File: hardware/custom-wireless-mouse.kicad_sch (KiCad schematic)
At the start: 34 parts, among them J1 SWD_HEADER, J2 B2B-XH-A, Q1 DMG2305UXQ, SW1 JS202011SCQN, SW2 D2FC-F-7N(20M), SW3 D2FC-F-7N(20M), SW4 D2FC-F-7N(20M), SW5 D2FC-F-7N(20M), U1 nRF52810-QCAA-T, U2 PMW3610DM-SUDU, U3 TLV61220DBVT, Y1 NX2016SA-32MHZ

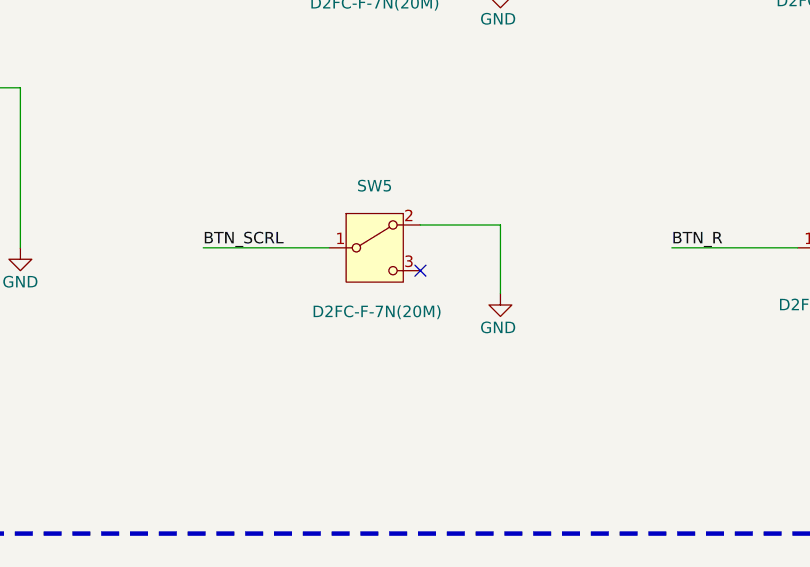
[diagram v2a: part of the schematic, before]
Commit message: Swap SW5 to a low-profile switch that clears the scroll wheel
SW5 (wheel middle-click) previously reused the same Omron D2FC-F-7N(20M)
as SW2-4, but that part's 6.5mm THT body doesn't fit underneath the
scroll wheel, which mounts on ENC1's shaft directly above it.

Deep-audited real, in-stock DigiKey.ca alternatives against the height
constraint and selected Omron B3U-1000P: 1.6mm actuator height, 2-pin
SPST-NO, exact-match footprint and 3D model already in KiCad's own
official library. Vendored the real datasheet, symbol, footprint, and
3D model; registered the new library; swapped SW5's schematic symbol,
footprint, and sourcing fields.

The old part's 3-pin COM/NO/NC wiring doesn't map onto the new part's
plain 2-pin SPST, so SW5's prior connections (to BTN_SCRL and GND) were
removed along with the old symbol rather than carried over incorrectly.
SW5 is intentionally left unwired pending manual rewiring and PCB
re-placement - documented in pinout.md and open-items.md. ERC confirms
the only fallout is the two now-expected unconnected pins on SW5.
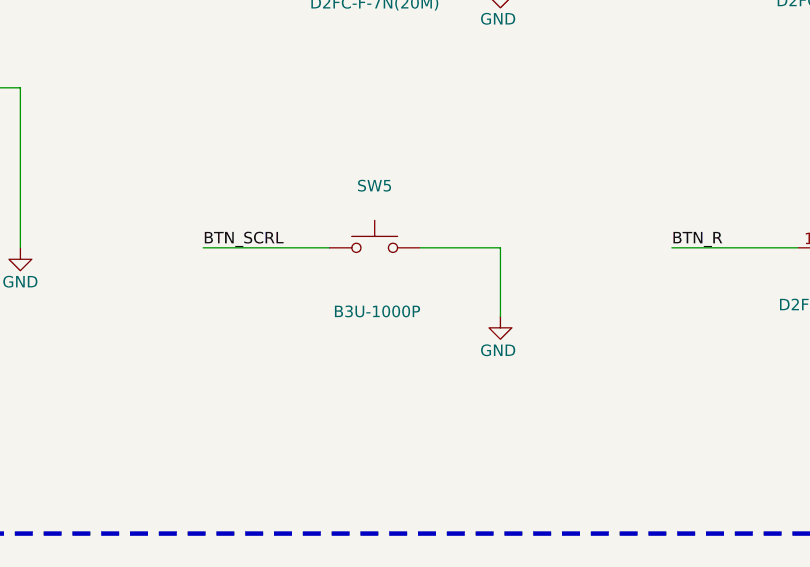
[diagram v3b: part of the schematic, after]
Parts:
- SW5: value D2FC-F-7N(20M) -> B3U-1000P; footprint omron-d2fc-f-7n:switch-tht-omron-d2fc-f-7n -> omron-b3u-1000p:switch-smd-omron-b3u-1000p; symbol omron-d2fc-f-7n:D2FC-F-7N-20M -> omron-b3u-1000p:B3U-1000P; DPN 39-D2FC-F-7N(20M)-ND -> SW1020CT-ND; MPN D2FC-F-7N(20M) -> B3U-1000P
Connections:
- no-connect marks 14 -> 13
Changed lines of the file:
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@@
 	)
 	(no_connect
-		(at 325.12 218.44)
-	)
-	(no_connect
 		(at 78.74 59.69)
 	)
@@
 	(wire
 		(pts
+			(xy 334.01 215.9) (xy 325.12 215.9)
+		)
+		(stroke
+			(width 0)
+			(type default)
+		)
+	)
+	(wire
+		(pts
 			(xy 113.03 213.36) (xy 139.7 213.36)
 		)
@@
 	(wire
 		(pts
-			(xy 314.96 215.9) (xy 300.99 215.9)
-		)
-		(stroke
-			(width 0)
-			(type default)
-		)
-	)
-	(wire
-		(pts
 			(xy 307.34 81.28) (xy 323.85 81.28)
 		)
@@
 	(wire
 		(pts
+			(xy 314.96 215.9) (xy 300.99 215.9)
+		)
+		(stroke
+			(width 0)
+			(type default)
+		)
+	)
+	(wire
+		(pts
 			(xy 346.71 35.56) (xy 346.71 38.1)
 		)
@@
 	(wire
 		(pts
+			(xy 334.01 215.9) (xy 334.01 223.52)
+		)
+		(stroke
+			(width 0)
+			(type default)
+		)
+	)
+	(wire
+		(pts
 			(xy 102.87 152.4) (xy 102.87 156.21)
 		)
@@
 	(wire
 		(pts
-			(xy 334.01 213.36) (xy 334.01 220.98)
-		)
-		(stroke
-			(width 0)
-			(type default)
-		)
-	)
-	(wire
-		(pts
 			(xy 246.38 100.33) (xy 229.87 100.33)
 		)
@@
 	(wire
 		(pts
-			(xy 334.01 213.36) (xy 325.12 213.36)
-		)
-		(stroke
-			(width 0)
-			(type default)
-		)
-	)
-	(wire
-		(pts
 			(xy 104.14 66.04) (xy 104.14 55.88)
 		)
@@
 		)
 	)
+	(label "BTN_SCRL"
+		(at 300.99 215.9 0)
+		(effects
+			(font
+				(size 1.27 1.27)
+			)
+			(justify left bottom)
+		)
+	)
 	(label "VBAT_SW"
 		(at 104.14 55.88 180)
@@
 		)
 	)
-	(label "BTN_SCRL"
-		(at 300.99 215.9 0)
-		(effects
-			(font
-				(size 1.27 1.27)
-			)
-			(justify left bottom)
-		)
-	)
 	(label "WHEEL_B"
 		(at 392.43 66.04 180)
@@
 	)
 	(symbol
-		(lib_id "omron-d2fc-f-7n:D2FC-F-7N-20M")
+		(lib_id "omron-b3u-1000p:B3U-1000P")
 		(at 320.04 215.9 0)
 		(unit 1)
@@
 			)
 		)
-		(property "Value" "D2FC-F-7N(20M)"
+		(property "Value" "B3U-1000P"
 			(at 320.294 223.012 0)
 			(show_name no)
@@
 			)
 		)
-		(property "Footprint" "omron-d2fc-f-7n:switch-tht-omron-d2fc-f-7n"
+		(property "Footprint" "omron-b3u-1000p:switch-smd-omron-b3u-1000p"
 			(at 320.04 215.9 0)
 			(hide yes)
@@
 			)
 		)
-		(property "Datasheet" "${KIPRJMOD}/datasheets/omron-d2f-family-datasheet.pdf"
+		(property "Datasheet" "${KIPRJMOD}/datasheets/omron-b3u-1000p-datasheet.pdf"
 			(at 320.04 215.9 0)
 			(hide yes)
@@
 			)
 		)
-		(property "Description" ""
+		(property "Description" "Ultra-small SMD tactile switch, SPST-NO, 1.6mm actuator height - low-profile wheel middle-click switch (swapped from D2FC-F-7N to clear the scroll wheel above it; UNWIRED, needs pin1/pin2 connected)"
 			(at 320.04 215.9 0)
+			(hide yes)
 			(show_name no)
 			(do_not_autoplace no)
@@
 			)
 		)
-		(property "MPN" "D2FC-F-7N(20M)"
+		(property "MPN" "B3U-1000P"
 			(at 0 0 0)
 			(hide yes)
@@
 			)
 		)
-		(property "DPN" "39-D2FC-F-7N(20M)-ND"
+		(property "DPN" "SW1020CT-ND"
 			(at 0 0 0)
 			(hide yes)
@@
 		(pin "2"
 		)
-		(pin "3"
-		)
 		(instances
 			(project "custom-wireless-mouse"
@@
 	(symbol
 		(lib_id "local:GND")
-		(at 334.01 220.98 0)
-		(unit 1)
-		(body_style 1)
-		(exclude_from_sim no)
-		(in_bom yes)
-		(on_board yes)
-		(in_pos_files yes)
-		(dnp no)
-		(property "Reference" "#PWR049"
-			(at 334.01 218.44 0)
-			(hide yes)
-			(show_name no)
-			(do_not_autoplace no)
-			(effects
-				(font
-					(size 1.27 1.27)
-				)
-			)
-		)
-		(property "Value" "GND"
-			(at 333.756 224.79 0)
-			(show_name no)
-			(do_not_autoplace no)
-			(effects
-				(font
-					(size 1.27 1.27)
-				)
-			)
-		)
-		(property "Footprint" ""
-			(at 334.01 220.98 0)
-			(hide yes)
-			(show_name no)
-			(do_not_autoplace no)
-			(effects
-				(font
-					(size 1.27 1.27)
-				)
-			)
-		)
-		(property "Datasheet" ""
-			(at 334.01 220.98 0)
-			(hide yes)
-			(show_name no)
-			(do_not_autoplace no)
-			(effects
-				(font
-					(size 1.27 1.27)
-				)
-			)
-		)
-		(property "Description" ""
-			(at 334.01 220.98 0)
-			(show_name no)
-			(do_not_autoplace no)
-			(effects
-				(font
-					(size 1.27 1.27)
-				)
-			)
-		)
-		(pin "1"
-		)
-		(instances
-			(project "custom-wireless-mouse"
-				(path "/d776ca83-3842-4947-ae63-5f40f232181f"
-					(reference "#PWR049")
-					(unit 1)
-				)
-			)
-		)
-	)
-	(symbol
-		(lib_id "local:GND")
 		(at 246.38 115.57 0)
 		(unit 1)
@@
 					(unit 1)
 				)
+			)
+		)
+	)
+	(symbol
+		(lib_id "local:GND")
+		(at 334.01 223.52 0)
+		(unit 1)
+		(body_style 1)
+		(exclude_from_sim no)
+		(in_bom yes)
+		(on_board yes)
+		(in_pos_files yes)
+		(dnp no)
+		(property "Reference" "#PWR041"
+			(at 334.01 220.98 0)
+			(hide yes)
+			(show_name no)
+			(do_not_autoplace no)
+			(effects
+				(font
+					(size 1.27 1.27)
+				)
+			)
+		)
+		(property "Value" "GND"
+			(at 333.756 227.33 0)
+			(show_name no)
+			(do_not_autoplace no)
+			(effects
+				(font
+					(size 1.27 1.27)
+				)
+			)
+		)
+		(property "Footprint" ""
+			(at 334.01 223.52 0)
+			(hide yes)
+			(show_name no)
+			(do_not_autoplace no)
+			(effects
+				(font
+					(size 1.27 1.27)
+				)
+			)
+		)
+		(property "Datasheet" ""
+			(at 334.01 223.52 0)
+			(hide yes)
+			(show_name no)
+			(do_not_autoplace no)
+			(effects
+				(font
+					(size 1.27 1.27)
+				)
+			)
+		)
+		(property "Description" ""
+			(at 334.01 223.52 0)
+			(show_name no)
+			(do_not_autoplace no)
+			(effects
+				(font
+					(size 1.27 1.27)
+				)
+			)
+		)
+		(pin "1"
+		)
+		(instances
+			(project "custom-wireless-mouse"
+				(path "/d776ca83-3842-4947-ae63-5f40f232181f"
+					(reference "#PWR041")
+					(unit 1)
+				)
